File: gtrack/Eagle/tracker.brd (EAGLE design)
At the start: 50.2 x 50 mm, 59 parts, among them IC1 STM32L152RBT, IC2 TPS73601, U2 SIM900, U3 MCP73831, X1 MINI-USB-32005-301

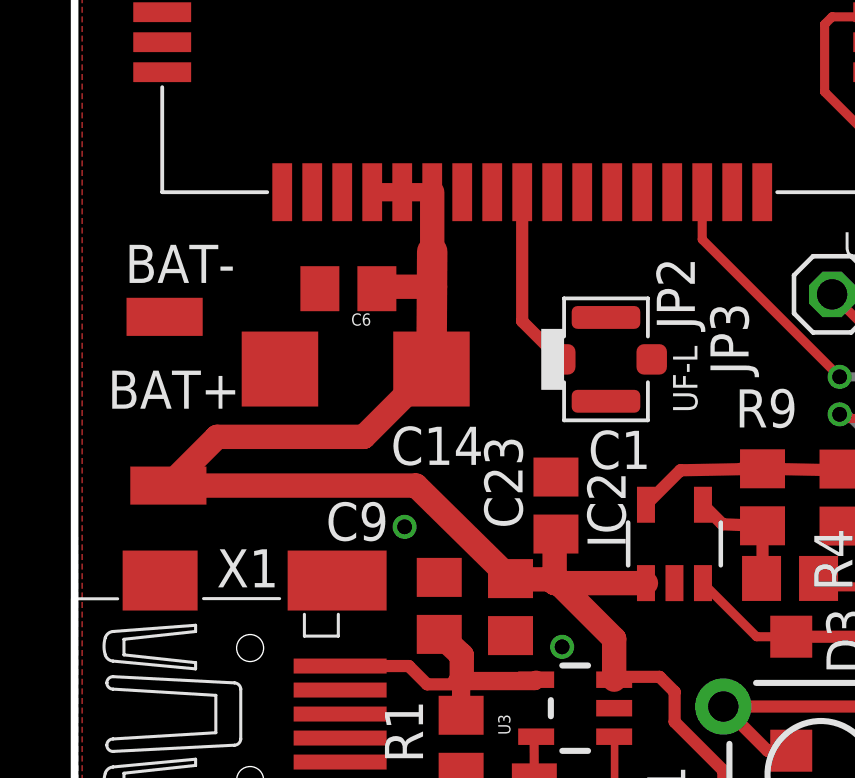
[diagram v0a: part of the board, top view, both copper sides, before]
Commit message: Add battery connector to PCB
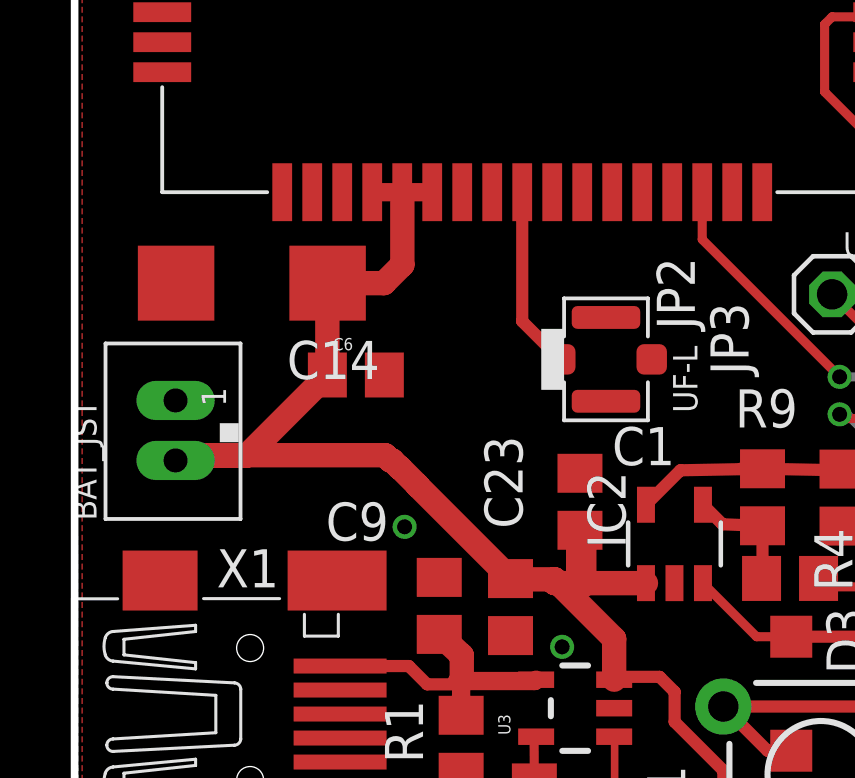
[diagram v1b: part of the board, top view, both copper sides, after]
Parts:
- removed BAT+, BAT-: (no value), wirepad:SMD1,27-2,54
- added BAT_JST: JST-PH_2-PIN_HEADER, SRG:JST_B2B-PH_HEADER
- moved C14 4.49 mm to (5.91, 20.6)
- moved C6 2.89 mm to (9.38, 17.6), turned to 0 degrees
- moved C1 0.81 mm to (16.8, 13.3)
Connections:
- net GND: now also BAT_JST.P1; no longer BAT-.1
- net GSM_VBAT: now also BAT_JST.P2; no longer BAT+.1
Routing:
- net GSM_VBAT: track 59.0 -> 54.5 mm
